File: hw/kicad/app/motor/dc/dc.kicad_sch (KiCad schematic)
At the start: 22 parts, among them J1 TOP, J2 Motor 1, J3 Motor 2, J4 Motor 3, J5 Motor 4, J6 BOTTUM, U1 DRV8870DDA, U2 DRV8870DDA, U3 DRV8870DDA, U4 DRV8870DDA

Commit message: 修改尺寸至45x45
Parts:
- C10, C11, C12, C2, C4, C6, C8, C9: footprint Capacitor_SMD:C_0603_1608Metric -> Capacitor_SMD:C_0805_2012Metric
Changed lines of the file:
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@@
       (effects (font (size 1.27 1.27)) (justify left))
     )
-    (property "Footprint" "Capacitor_SMD:C_0603_1608Metric" (at 228.2952 143.51 0)
+    (property "Footprint" "Capacitor_SMD:C_0805_2012Metric" (at 228.2952 143.51 0)
       (effects (font (size 1.27 1.27)) hide)
     )
@@
       (effects (font (size 1.27 1.27)) (justify left))
     )
-    (property "Footprint" "Capacitor_SMD:C_0603_1608Metric" (at 115.9002 103.505 0)
+    (property "Footprint" "Capacitor_SMD:C_0805_2012Metric" (at 115.9002 103.505 0)
       (effects (font (size 1.27 1.27)) hide)
     )
@@
       (effects (font (size 1.27 1.27)) (justify left))
     )
-    (property "Footprint" "Capacitor_SMD:C_0603_1608Metric" (at 114.6302 46.355 0)
+    (property "Footprint" "Capacitor_SMD:C_0805_2012Metric" (at 114.6302 46.355 0)
       (effects (font (size 1.27 1.27)) hide)
     )
@@
       (effects (font (size 1.27 1.27)) (justify left))
     )
-    (property "Footprint" "Capacitor_SMD:C_0603_1608Metric" (at 179.7812 155.321 0)
+    (property "Footprint" "Capacitor_SMD:C_0805_2012Metric" (at 179.7812 155.321 0)
       (effects (font (size 1.27 1.27)) hide)
     )
@@
       (effects (font (size 1.27 1.27)) (justify left))
     )
-    (property "Footprint" "Capacitor_SMD:C_0603_1608Metric" (at 116.5352 153.67 0)
+    (property "Footprint" "Capacitor_SMD:C_0805_2012Metric" (at 116.5352 153.67 0)
       (effects (font (size 1.27 1.27)) hide)
     )
@@
       (effects (font (size 1.27 1.27)) (justify left))
     )
-    (property "Footprint" "Capacitor_SMD:C_0603_1608Metric" (at 66.4972 113.919 0)
+    (property "Footprint" "Capacitor_SMD:C_0805_2012Metric" (at 66.4972 113.919 0)
       (effects (font (size 1.27 1.27)) hide)
     )
@@
       (effects (font (size 1.27 1.27)) (justify left))
     )
-    (property "Footprint" "Capacitor_SMD:C_0603_1608Metric" (at 65.3542 57.531 0)
+    (property "Footprint" "Capacitor_SMD:C_0805_2012Metric" (at 65.3542 57.531 0)
       (effects (font (size 1.27 1.27)) hide)
     )
@@
       (effects (font (size 1.27 1.27)) (justify left))
     )
-    (property "Footprint" "Capacitor_SMD:C_0603_1608Metric" (at 66.7512 166.878 0)
-      (effects (font (size 1.27 1.27)) hide)
-    )
+    (property "Footprint" "Capacitor_SMD:C_0805_2012Metric" (at 66.7512 166.878 0)
+      (effects (font (size 1.27 1.27)) hide)
+    )

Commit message: 更新read me
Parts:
- J2, J3, J4, J5: footprint Connector_JST:JST_GH_BM04B-GHS-TBT_1x04-1MP_P1.25mm_Vertical -> JST_BM04B-GHS-TBT(LF)(SN)(N)
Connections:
- net GND: now also J2.MP (SHIELD), J3.MP (SHIELD), J4.MP (SHIELD), J5.MP (SHIELD); no longer J2.S1 (SHIELD), J2.S2 (SHIELD), J3.S1 (SHIELD), J3.S2 (SHIELD), J4.S1 (SHIELD), J4.S2 (SHIELD), J5.S1 (SHIELD), J5.S2 (SHIELD)
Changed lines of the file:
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@@
     (effects (font (size 1.27 1.27)) (justify left bottom))
   )
-  (symbol (lib_id "JST-GHS-1.25-BM04B:BM04B-GHS-TBT(LF)(SN)(N)") (at 149.86 40.64 0) (unit 1)
+  (symbol (lib_name "BM04B-GHS-TBT(LF)(SN)(N)_1") (lib_id "JST-GHS-1.25-BM04B:BM04B-GHS-TBT(LF)(SN)(N)") (at 149.86 40.64 0) (unit 1)
     (in_bom yes) (on_board yes) (dnp no) (fields_autoplaced)
     (property "Reference" "J2" (at 156.21 40.64 0)
@@
       (effects (font (size 1.27 1.27)) (justify left))
     )
-    (property "Footprint" "Connector_JST:JST_GH_BM04B-GHS-TBT_1x04-1MP_P1.25mm_Vertical" (at 149.86 40.64 0)
+    (property "Footprint" "JST_BM04B-GHS-TBT(LF)(SN)(N)" (at 149.86 40.64 0)
       (effects (font (size 1.27 1.27)) (justify bottom) hide)
     )
@@
     (pin "3")
     (pin "4")
-    (pin "S1")
-    (pin "S2")
+    (pin "MP")
+    (pin "MP")
     (instances
       (project "dc"
@@
       (effects (font (size 1.27 1.27)) (justify left))
     )
-    (property "Footprint" "Connector_JST:JST_GH_BM04B-GHS-TBT_1x04-1MP_P1.25mm_Vertical" (at 263.525 137.795 0)
+    (property "Footprint" "JST_BM04B-GHS-TBT(LF)(SN)(N)" (at 263.525 137.795 0)
       (effects (font (size 1.27 1.27)) (justify bottom) hide)
     )
@@
     (pin "3")
     (pin "4")
-    (pin "S1")
-    (pin "S2")
+    (pin "MP")
+    (pin "MP")
     (instances
       (project "dc"
@@
     )
   )
-  (symbol (lib_id "JST-GHS-1.25-BM04B:BM04B-GHS-TBT(LF)(SN)(N)") (at 151.13 97.79 0) (unit 1)
+  (symbol (lib_name "BM04B-GHS-TBT(LF)(SN)(N)_2") (lib_id "JST-GHS-1.25-BM04B:BM04B-GHS-TBT(LF)(SN)(N)") (at 151.13 97.79 0) (unit 1)
     (in_bom yes) (on_board yes) (dnp no) (fields_autoplaced)
     (property "Reference" "J3" (at 157.48 97.79 0)
@@
       (effects (font (size 1.27 1.27)) (justify left))
     )
-    (property "Footprint" "Connector_JST:JST_GH_BM04B-GHS-TBT_1x04-1MP_P1.25mm_Vertical" (at 151.13 97.79 0)
+    (property "Footprint" "JST_BM04B-GHS-TBT(LF)(SN)(N)" (at 151.13 97.79 0)
       (effects (font (size 1.27 1.27)) (justify bottom) hide)
     )
@@
     (pin "3")
     (pin "4")
-    (pin "S1")
-    (pin "S2")
+    (pin "MP")
+    (pin "MP")
     (instances
       (project "dc"
@@
     )
   )
-  (symbol (lib_id "JST-GHS-1.25-BM04B:BM04B-GHS-TBT(LF)(SN)(N)") (at 151.765 147.955 0) (unit 1)
+  (symbol (lib_name "BM04B-GHS-TBT(LF)(SN)(N)_3") (lib_id "JST-GHS-1.25-BM04B:BM04B-GHS-TBT(LF)(SN)(N)") (at 151.765 147.955 0) (unit 1)
     (in_bom yes) (on_board yes) (dnp no) (fields_autoplaced)
     (property "Reference" "J4" (at 158.75 147.955 0)
@@
       (effects (font (size 1.27 1.27)) (justify left))
     )
-    (property "Footprint" "Connector_JST:JST_GH_BM04B-GHS-TBT_1x04-1MP_P1.25mm_Vertical" (at 151.765 147.955 0)
+    (property "Footprint" "JST_BM04B-GHS-TBT(LF)(SN)(N)" (at 151.765 147.955 0)
       (effects (font (size 1.27 1.27)) (justify bottom) hide)
     )
@@
     (pin "3")
     (pin "4")
-    (pin "S1")
-    (pin "S2")
-    (instances
-      (project "dc"
+    (pin "MP")
+    (pin "MP")
+    (instances
+      (project "dc"

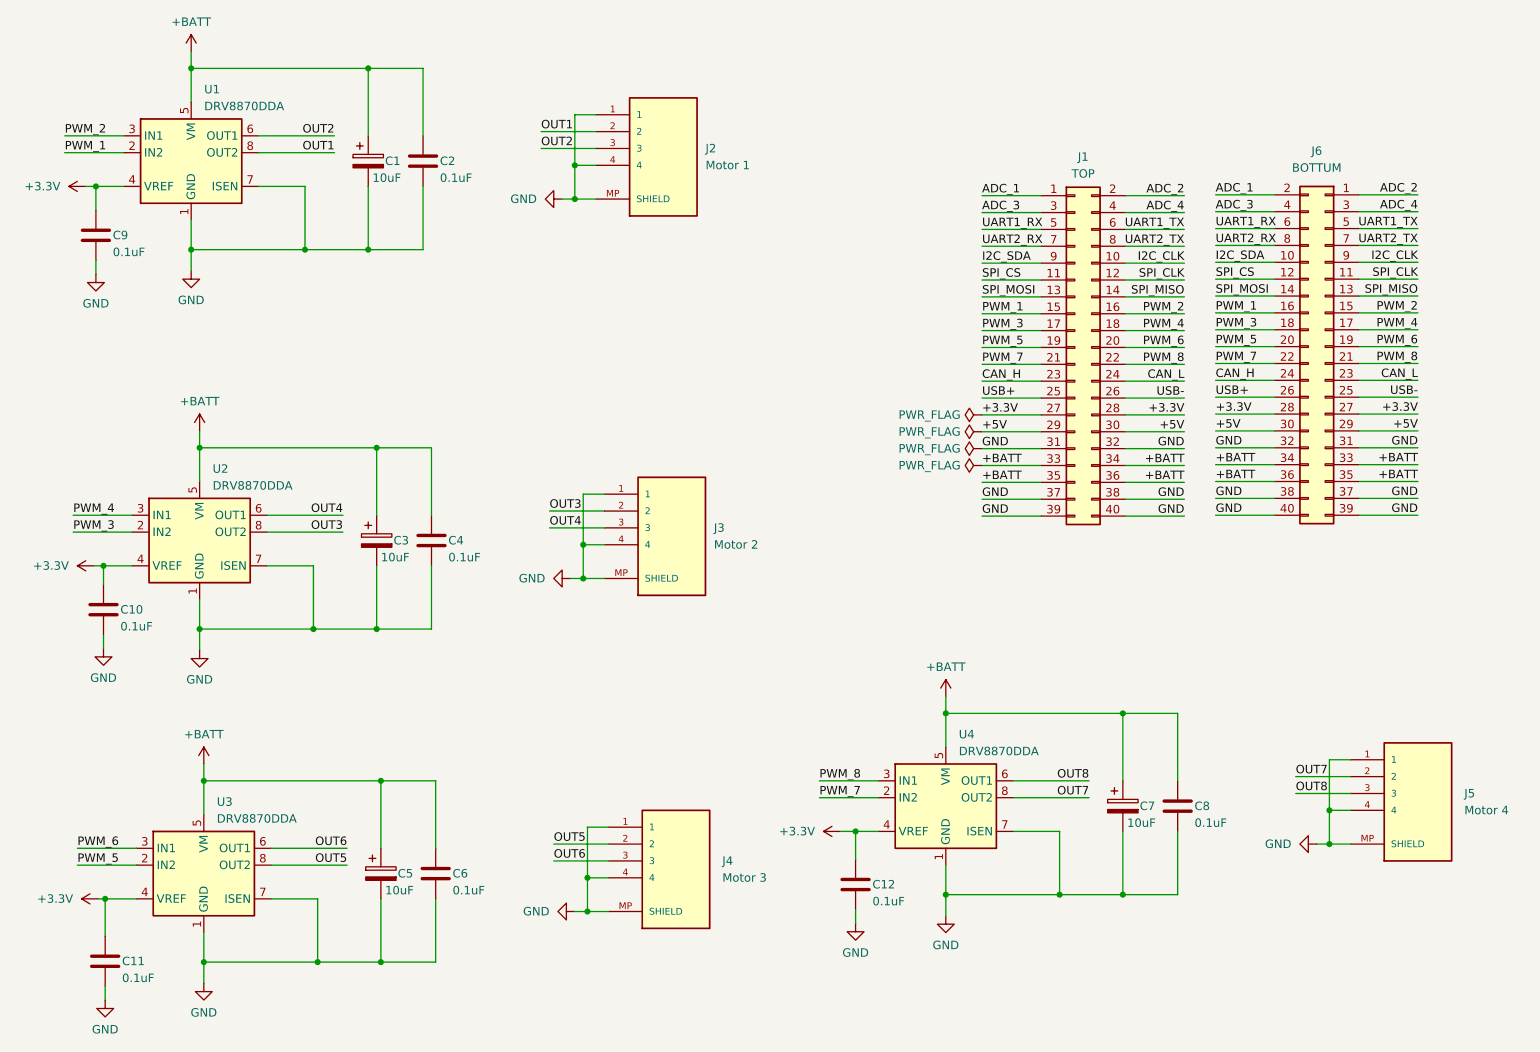
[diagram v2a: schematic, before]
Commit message: 第二次打样的整改；dc motor改成了三路 io不够做不了四路；
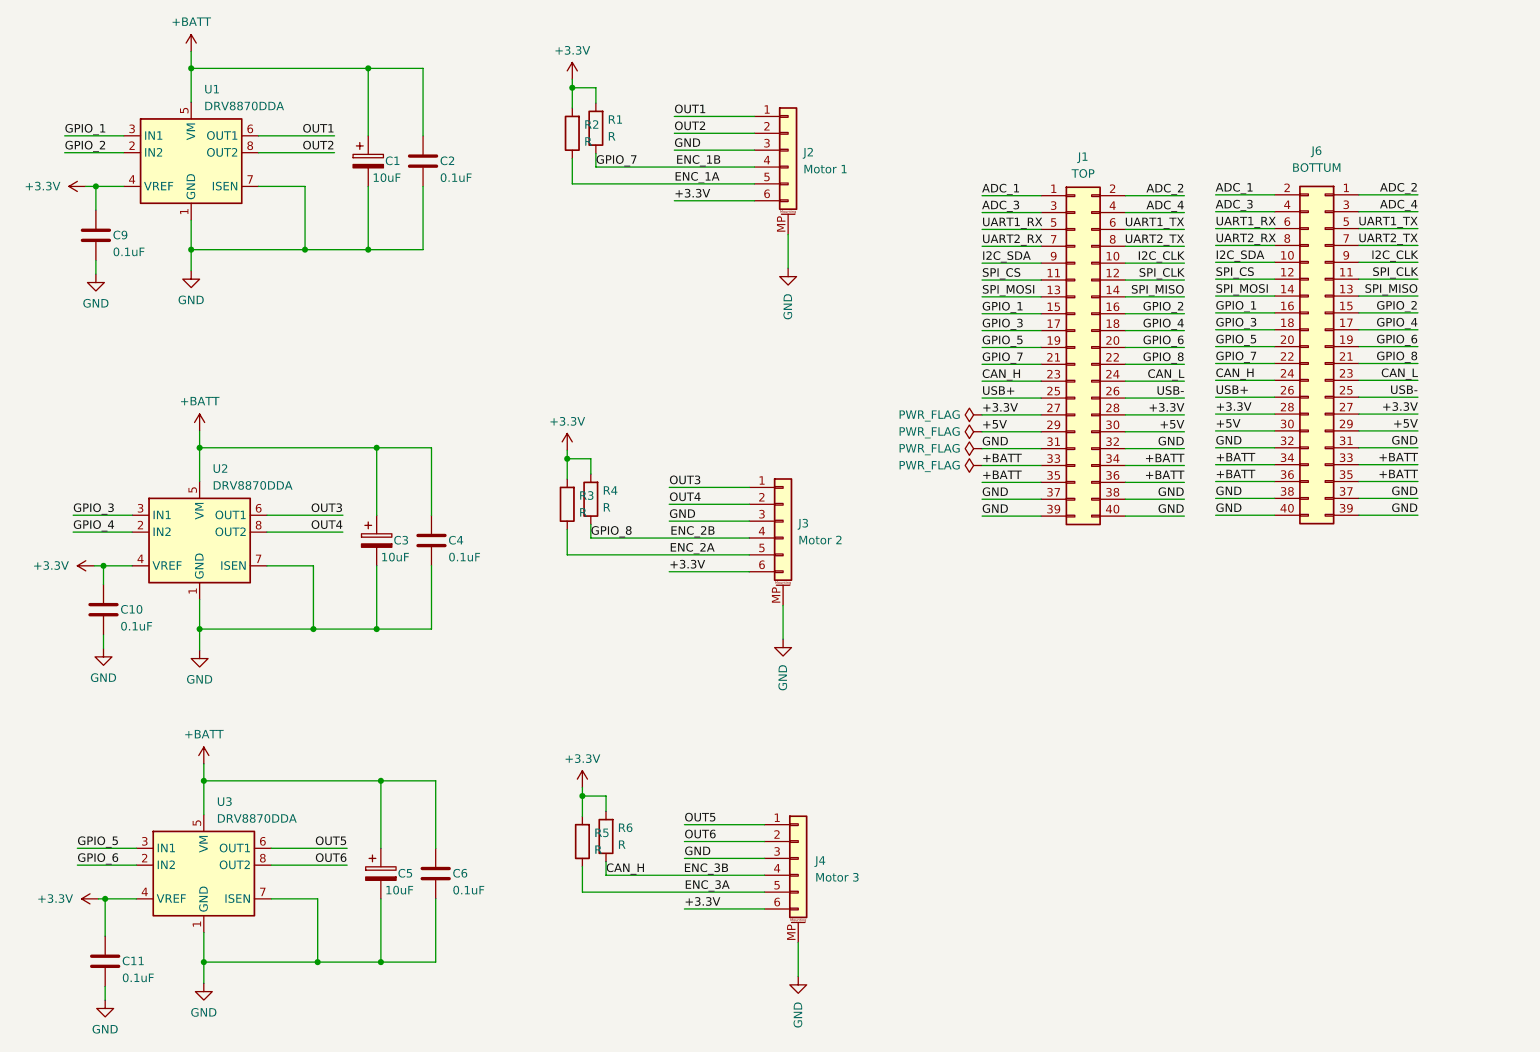
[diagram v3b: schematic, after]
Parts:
- removed C12, C8: 0.1uF, Capacitor_SMD:C_0805_2012Metric, symbol Device:C
- removed C7: 10uF, Capacitor_SMD:CP_Elec_6.3x5.4, symbol Device:C_Polarized
- removed J2: Motor 1, JST_BM04B-GHS-TBT(LF)(SN)(N), symbol JST-GHS-1.25-BM04B:BM04B-GHS-TBT(LF)(SN)(N)
- removed J3: Motor 2, JST_BM04B-GHS-TBT(LF)(SN)(N), symbol JST-GHS-1.25-BM04B:BM04B-GHS-TBT(LF)(SN)(N)
- removed J4: Motor 3, JST_BM04B-GHS-TBT(LF)(SN)(N), symbol JST-GHS-1.25-BM04B:BM04B-GHS-TBT(LF)(SN)(N)
- removed J5: Motor 4, JST_BM04B-GHS-TBT(LF)(SN)(N), symbol JST-GHS-1.25-BM04B:BM04B-GHS-TBT(LF)(SN)(N)
- removed U4: DRV8870DDA, Package_SO:Texas_HTSOP-8-1EP_3.9x4.9mm_P1.27mm_EP2.95x4.9mm_Mask2.4x3.1mm_ThermalVias, symbol Driver_Motor:DRV8870DDA
- added J2: Motor 1, Connector_JST:JST_GH_SM06B-GHS-TB_1x06-1MP_P1.25mm_Horizontal, symbol Connector_Generic_MountingPin:Conn_01x06_MountingPin
- added J3: Motor 2, Connector_JST:JST_GH_SM06B-GHS-TB_1x06-1MP_P1.25mm_Horizontal, symbol Connector_Generic_MountingPin:Conn_01x06_MountingPin
- added J4: Motor 3, Connector_JST:JST_GH_SM06B-GHS-TB_1x06-1MP_P1.25mm_Horizontal, symbol Connector_Generic_MountingPin:Conn_01x06_MountingPin
- added R1, R2, R3, R4, R5, R6: R, Resistor_SMD:R_0805_2012Metric, symbol Device:R
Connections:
- net +3.3V: now also J2.6 (Pin_6), J3.6 (Pin_6), J4.6 (Pin_6), R1.2, R2.2, R3.2, R4.2, R5.2, R6.2
- net CAN_H: now also J4.4 (Pin_4), R6.1
- net GND: now also J2.3 (Pin_3), J2.MP (MountPin), J3.3 (Pin_3), J3.MP (MountPin), J4.3 (Pin_3), J4.MP (MountPin)
- net OUT1: now also U1.6 (OUT1), J2.1 (Pin_1); no longer U1.8 (OUT2)
- net OUT2: now also U1.8 (OUT2), J2.2 (Pin_2); no longer U1.6 (OUT1)
- net OUT3: now also U2.6 (OUT1), J3.1 (Pin_1); no longer U2.8 (OUT2)
- net OUT4: now also U2.8 (OUT2), J3.2 (Pin_2); no longer U2.6 (OUT1)
- net OUT5: now also U3.6 (OUT1), J4.1 (Pin_1); no longer U3.8 (OUT2)
- net OUT6: now also U3.8 (OUT2), J4.2 (Pin_2); no longer U3.6 (OUT1)
- net PWM_1 renamed GPIO_1
- net GPIO_1: now also U1.3 (IN1); no longer U1.2 (IN2)
- net PWM_2 renamed GPIO_2
- net GPIO_2: now also U1.2 (IN2); no longer U1.3 (IN1)
- net PWM_3 renamed GPIO_3
- net GPIO_3: now also U2.3 (IN1); no longer U2.2 (IN2)
- net PWM_4 renamed GPIO_4
- net GPIO_4: now also U2.2 (IN2); no longer U2.3 (IN1)
- net PWM_5 renamed GPIO_5
- net GPIO_5: now also U3.3 (IN1); no longer U3.2 (IN2)
- net PWM_6 renamed GPIO_6
- net GPIO_6: now also U3.2 (IN2); no longer U3.3 (IN1)
- net PWM_7 renamed ENC_1B
- net ENC_1B: now also J2.4 (Pin_4), R1.1
- net PWM_8 renamed ENC_2B
- net ENC_2B: now also J3.4 (Pin_4), R4.1
- new net ENC_1A: J2.5 (Pin_5), R2.1
- new net ENC_2A: J3.5 (Pin_5), R3.1
- new net ENC_3A: J4.5 (Pin_5), R5.1
